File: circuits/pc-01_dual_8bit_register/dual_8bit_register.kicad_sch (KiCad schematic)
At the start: 34 parts, among them J1 Conn_01x10, U1 74HC273, U2 74HC273, U3 74HC244, U4 74HC244, U5 74HC244, U6 74HC244

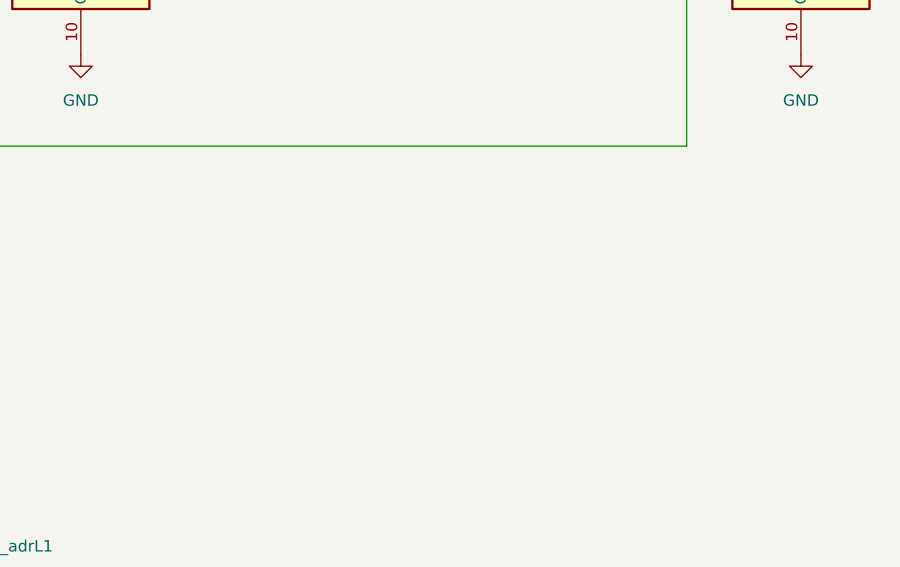
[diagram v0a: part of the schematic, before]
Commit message: add filter and decoupling capacitors to all boards
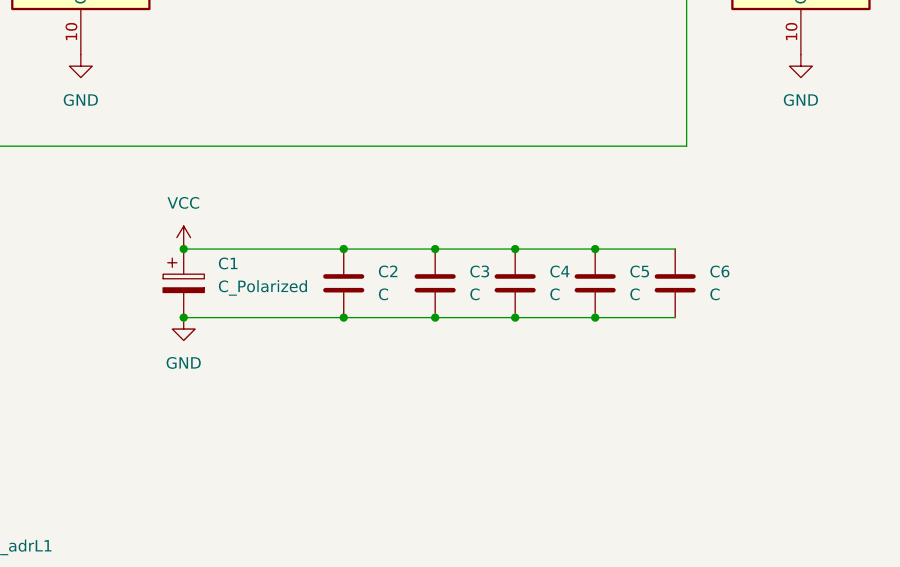
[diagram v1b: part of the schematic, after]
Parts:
- added C1: C_Polarized, Capacitor_SMD:CP_Elec_5x5.3, symbol Device:C_Polarized
- added C2, C3, C4, C5, C6: C, Capacitor_SMD:C_0603_1608Metric, symbol Device:C
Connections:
- net GND: now also C1.2, C2.2, C3.2, C4.2, C5.2, C6.2
- net VCC: now also C1.1, C2.1, C3.1, C4.1, C5.1, C6.1
